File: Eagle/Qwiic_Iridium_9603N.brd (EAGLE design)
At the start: 50.8 x 50.8 mm, 90 parts, among them J1 IRIDIUM_9603N, J3 PTH, J6 ISP, J7 U.FL, Q2 5.8A/30V/35mΩ, U1 ATTINY841SOIC, U2 LTC3225EDDB#TRMPBF, U3 ADM4210-1

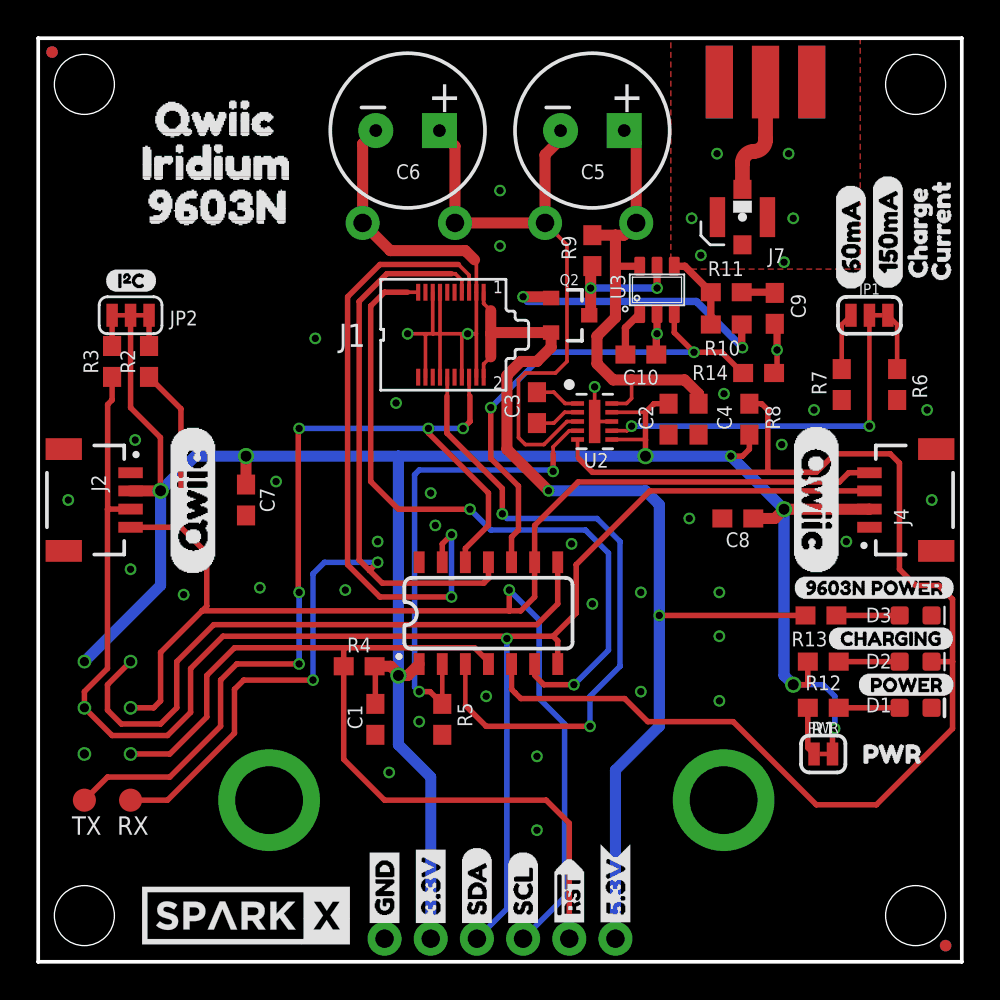
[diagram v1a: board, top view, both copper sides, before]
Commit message: Add ignore. Remove old backup files. Move TPs to bottom of board.
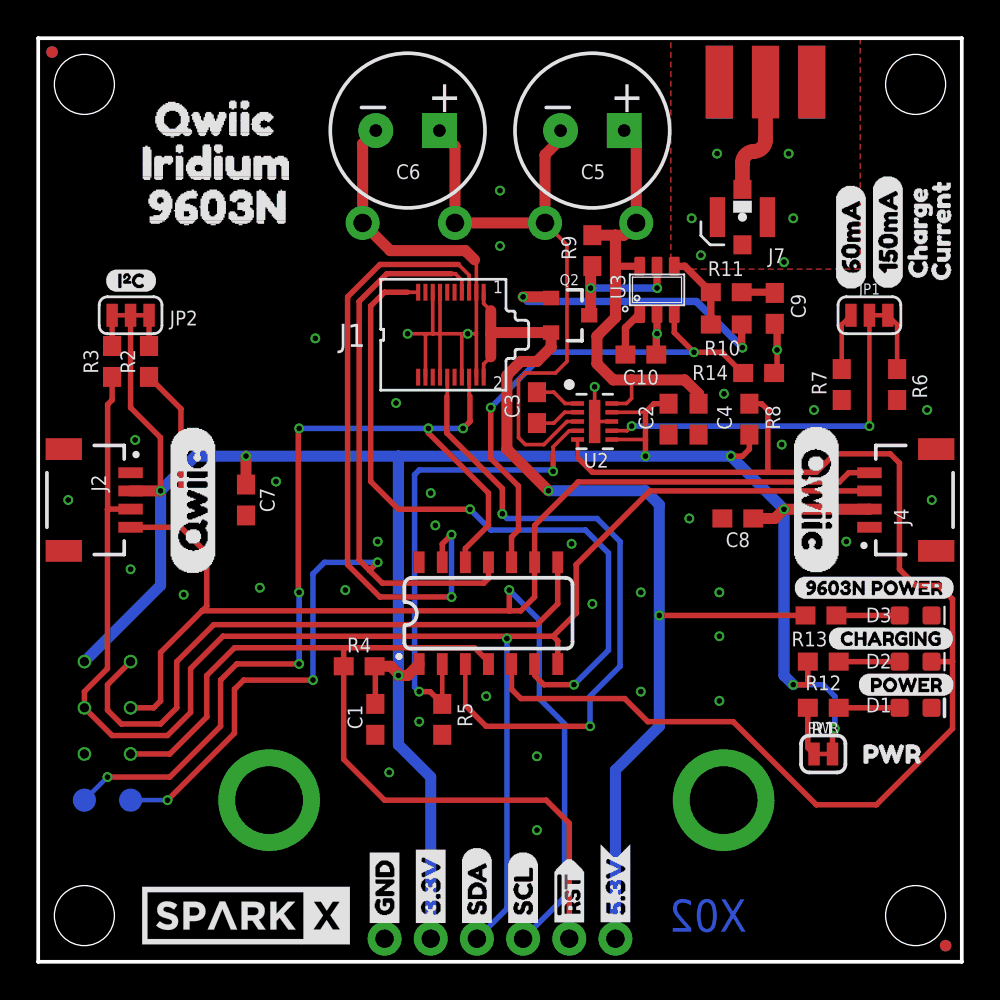
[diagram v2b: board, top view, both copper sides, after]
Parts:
- J2, J4: value (none) -> QWIIC_RIGHT_ANGLE
- flipped RX to the bottom
- flipped TX to the bottom
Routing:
- net RX(OUT): vias 2 -> 3
- net TX(IN): vias 5 -> 6
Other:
- board text added: "X02"
- board text removed: "X0.1"

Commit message: Update connector footprint: reduce cream, extend copper, remove extra silk.
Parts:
- J2, J4: value QWIIC_RIGHT_ANGLE -> (none)
- JP10, JP3, JP4, JP9: device SparkFun:STAND-OFF -> SparkFun-Hardware:STAND-OFF
- JP5, JP6, JP7, JP8: value FIDUCIALUFIDUCIAL -> FIDUCIAL1X2; device SparkFun:MICRO-FIDUCIAL -> SparkFun-Aesthetics:FIDUCIAL-1X2
- R1, R12: device SparkFun-Resistors:0603 -> Qwiic_Iridium_9603N:0603
- U3: device ADM4210:TSOT6 -> Qwiic_Iridium_9603N:TSOT6
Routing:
- net GND: track 42.4 -> 43.0 mm

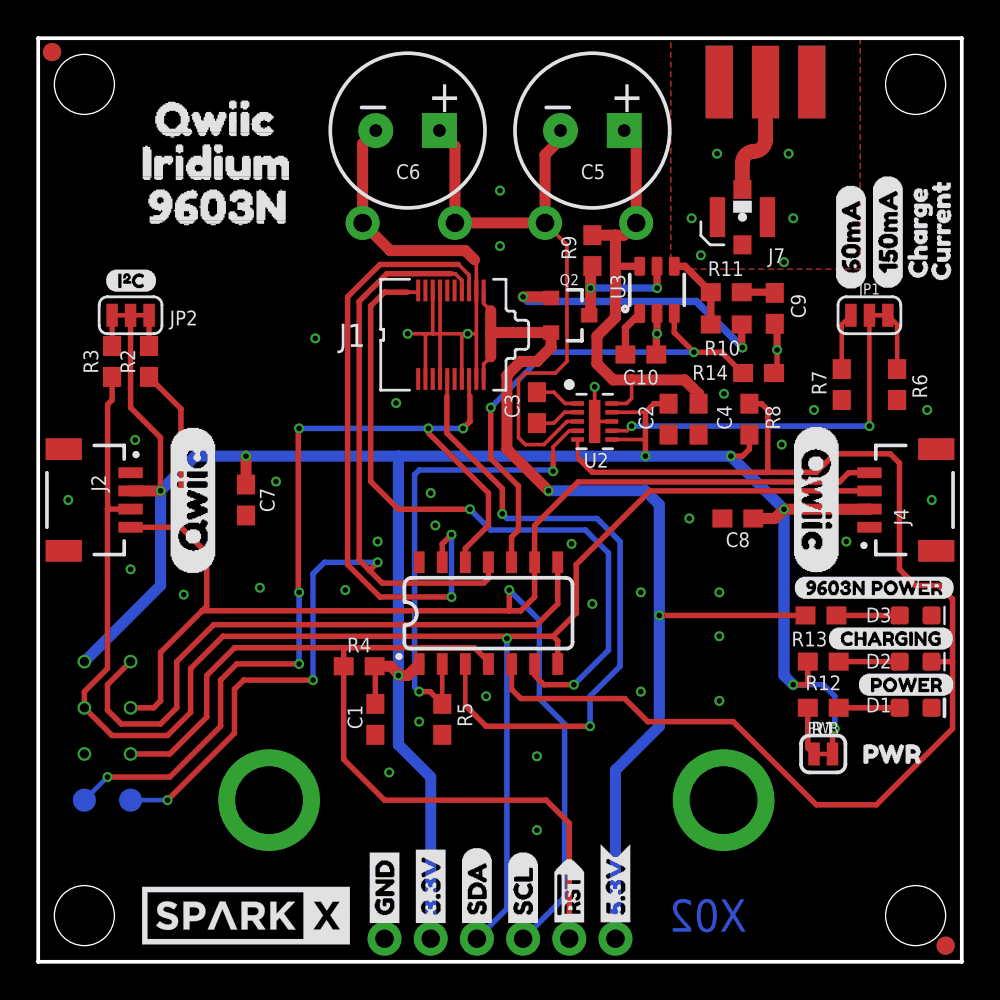
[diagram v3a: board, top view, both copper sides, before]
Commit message: Change connector to use SMD reflowable standoffs
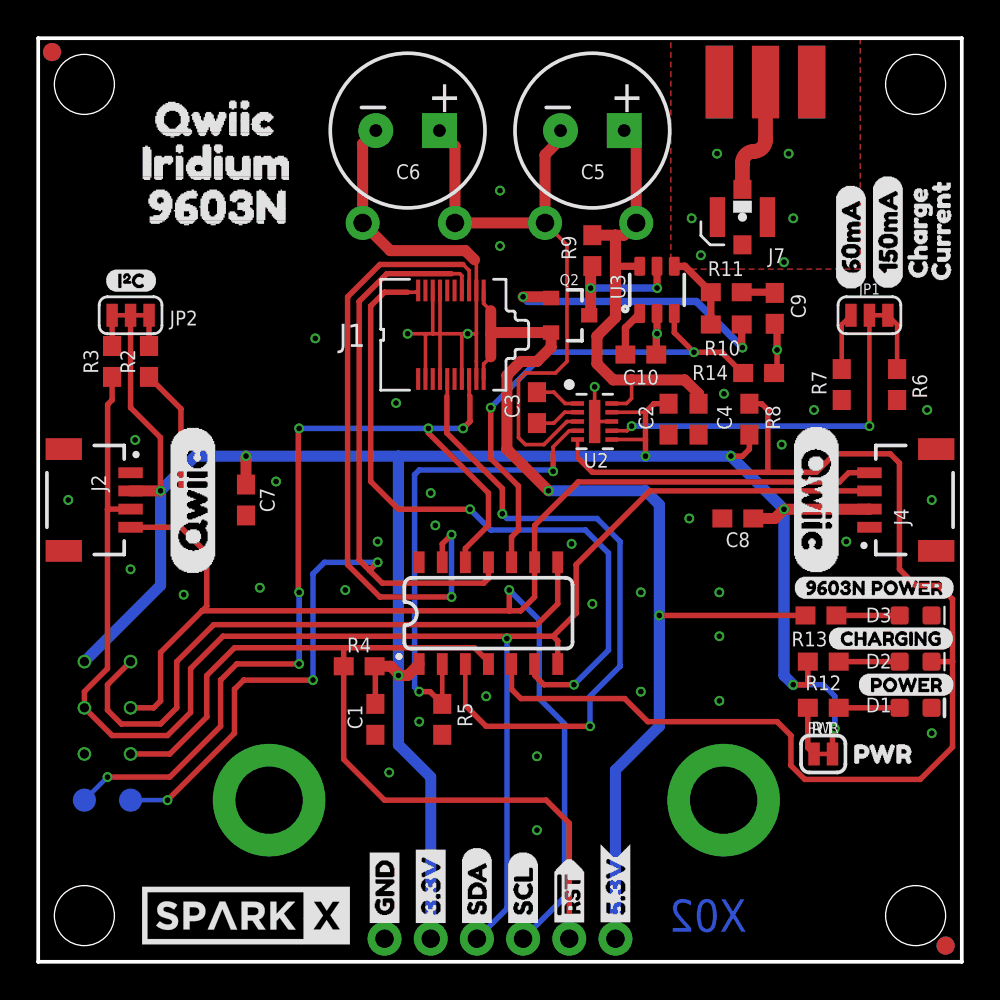
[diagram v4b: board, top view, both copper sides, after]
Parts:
- moved U$31 0.51 mm to (43.6, 11.4)
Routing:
- net GND: vias 44 -> 45
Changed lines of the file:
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@@
 <layer number="44" name="Drills" color="7" fill="1" visible="no" active="yes"/>
 <layer number="45" name="Holes" color="7" fill="1" visible="yes" active="yes"/>
-<layer number="46" name="Milling" color="3" fill="1" visible="yes" active="yes"/>
+<layer number="46" name="Milling" color="3" fill="1" visible="no" active="yes"/>
 <layer number="47" name="Measures" color="7" fill="1" visible="no" active="yes"/>
 <layer number="48" name="Document" color="7" fill="1" visible="no" active="yes"/>
-<layer number="49" name="Reference" color="7" fill="1" visible="no" active="yes"/>
+<layer number="49" name="Reference" color="7" fill="1" visible="yes" active="yes"/>
 <layer number="50" name="dxf" color="7" fill="1" visible="no" active="yes"/>
 <layer number="51" name="tDocu" color="6" fill="1" visible="yes" active="yes"/>
@@
 <element name="U$29" library="SparkX" package="SPARKX-LARGE" value="" x="8.89" y="41.91" smashed="yes" rot="MR0"/>
 <element name="U$30" library="SparkX" package="SPARKX-LARGE" value="" x="11.43" y="2.54" smashed="yes"/>
-<element name="U$31" library="buzzard_labels (7)" package="_PWR1" value="" x="44.069" y="11.43" smashed="yes"/>
+<element name="U$31" library="buzzard_labels (7)" package="_PWR1" value="" x="43.561" y="11.43" smashed="yes"/>
 <element name="U$32" library="buzzard_labels (7)" package="5#3V0" value="" x="31.75" y="1.651" smashed="yes" rot="R90"/>
 <element name="U$11" library="buzzard_labels (7)" package="5#3V0" value="" x="31.75" y="1.651" smashed="yes" rot="MR90"/>
@@
 <contactref element="J1" pad="14"/>
 <contactref element="J1" pad="18"/>
-<wire x1="24.1" y1="32.055" x2="24.1" y2="34.544" width="0.2032" layer="1"/>
+<wire x1="24.1" y1="32.055" x2="24.1" y2="33.02" width="0.2032" layer="1"/>
+<wire x1="24.1" y1="33.02" x2="24.1" y2="34.544" width="0.2032" layer="1"/>
 <wire x1="24.1" y1="34.544" x2="24.1" y2="36.925" width="0.2032" layer="1"/>
 <wire x1="23.622" y1="34.544" x2="24.1" y2="34.544" width="0.2032" layer="1"/>
@@
 <via x="30.607" y="31.623" extent="1-16" drill="0.3048"/>
 <wire x1="30.607" y1="29.718" x2="30.607" y2="31.623" width="0.2032" layer="1"/>
+<wire x1="24.1" y1="33.02" x2="24.1" y2="33.02" width="0.2032" layer="1"/>
+<via x="49.149" y="12.573" extent="1-16" drill="0.3048"/>
 </signal>
 <signal name="SCL">
@@
 <wire x1="17.018" y1="36.576" x2="17.018" y2="21.844" width="0.3048" layer="1"/>
 <wire x1="17.018" y1="36.576" x2="18.796" y2="38.354" width="0.3048" layer="1"/>
-<wire x1="18.796" y1="38.354" x2="23.114" y2="38.354" width="0.3048" layer="1"/>
-<wire x1="23.69998125" y1="37.76801875" x2="23.114" y2="38.354" width="0.2032" layer="1"/>
+<wire x1="18.796" y1="38.354" x2="23.368" y2="38.354" width="0.3048" layer="1"/>
+<wire x1="23.69998125" y1="38.02201875" x2="23.368" y2="38.354" width="0.2032" layer="1"/>
 <contactref element="J1" pad="5"/>
 <wire x1="23.7" y1="36.925" x2="23.69998125" y2="36.82501875" width="0.2032" layer="1"/>
-<wire x1="23.69998125" y1="36.82501875" x2="23.69998125" y2="37.76801875" width="0.2032" layer="1"/>
+<wire x1="23.69998125" y1="36.82501875" x2="23.69998125" y2="38.02201875" width="0.2032" layer="1"/>
 <wire x1="18.796" y1="20.066" x2="22.733" y2="20.066" width="0.3048" layer="1"/>
 <via x="22.733" y="20.066" extent="1-16" drill="0.3048"/>
@@
 </signal>
 <signal name="RX(OUT)">
-<wire x1="22.733" y1="37.846" x2="22.93823125" y2="37.846" width="0.2032" layer="1"/>
-<wire x1="23.29998125" y1="37.48425" x2="22.93823125" y2="37.846" width="0.2032" layer="1"/>
+<wire x1="22.733" y1="37.846" x2="23.19223125" y2="37.846" width="0.2032" layer="1"/>
+<wire x1="23.29998125" y1="37.73825" x2="23.19223125" y2="37.846" width="0.2032" layer="1"/>
 <wire x1="18.923" y1="20.828" x2="18.2245" y2="21.5265" width="0.3048" layer="1"/>
 <wire x1="18.2245" y1="21.5265" x2="17.653" y2="22.098" width="0.3048" layer="1"/>
@@
 <contactref element="J1" pad="7"/>
 <wire x1="23.3" y1="36.925" x2="23.29998125" y2="36.82501875" width="0.2032" layer="1"/>
-<wire x1="23.29998125" y1="36.82501875" x2="23.29998125" y2="37.48425" width="0.2032" layer="1"/>
+<wire x1="23.29998125" y1="36.82501875" x2="23.29998125" y2="37.73825" width="0.2032" layer="1"/>
 <wire x1="24.511" y1="20.828" x2="24.765" y2="21.082" width="0.3048" layer="1"/>
 <wire x1="24.511" y1="20.828" x2="18.923" y2="20.828" width="0.3048" layer="1"/>
@@
 <wire x1="48.26" y1="20.701" x2="49.53" y2="20.701" width="0.3048" layer="1"/>
 <wire x1="49.53" y1="20.701" x2="50.292" y2="19.939" width="0.3048" layer="1"/>
-<wire x1="50.292" y1="12.827" x2="46.101" y2="8.636" width="0.3048" layer="1"/>
-<wire x1="46.101" y1="8.636" x2="42.799" y2="8.636" width="0.3048" layer="1"/>
-<wire x1="42.799" y1="8.636" x2="38.227" y2="13.208" width="0.3048" layer="1"/>
-<wire x1="33.528" y1="13.208" x2="38.227" y2="13.208" width="0.3048" layer="1"/>
+<wire x1="50.292" y1="11.811" x2="48.514" y2="10.033" width="0.3048" layer="1"/>
+<wire x1="42.164" y1="10.033" x2="48.514" y2="10.033" width="0.3048" layer="1"/>
 <wire x1="30.48" y1="26.924" x2="40.132" y2="26.924" width="0.3048" layer="1"/>
 <wire x1="40.132" y1="26.924" x2="42.799" y2="26.924" width="0.3048" layer="1"/>
 <wire x1="50.292" y1="19.939" x2="50.292" y2="16.51" width="0.3048" layer="1"/>
-<wire x1="50.292" y1="16.51" x2="50.292" y2="12.827" width="0.3048" layer="1"/>
+<wire x1="50.292" y1="16.51" x2="50.292" y2="11.811" width="0.3048" layer="1"/>
 <wire x1="49.137" y1="16.51" x2="50.292" y2="16.51" width="0.3048" layer="1"/>
 <wire x1="39.116" y1="30.695" x2="39.79" y2="30.695" width="0.3048" layer="1"/>
@@
 <contactref element="U1" pad="5"/>
 <wire x1="26.035" y1="14.986" x2="26.035" y2="16.377" width="0.3048" layer="1"/>
+<wire x1="41.402" y1="12.446" x2="41.402" y2="10.795" width="0.3048" layer="1"/>
+<wire x1="41.402" y1="10.795" x2="42.164" y2="10.033" width="0.3048" layer="1"/>
+<wire x1="33.528" y1="13.208" x2="40.64" y2="13.208" width="0.3048" layer="1"/>
+<wire x1="40.64" y1="13.208" x2="41.402" y2="12.446" width="0.3048" layer="1"/>
 </signal>
 <signal name="N$11">
@@
 <via x="29.464" y="15.24" extent="1-16" drill="0.3048"/>
 <contactref element="J1" pad="19"/>
-<wire x1="20.9" y1="36.925" x2="20.895" y2="36.83" width="0.2032" layer="1"/>
-<wire x1="20.895" y1="36.83" x2="20.32" y2="36.83" width="0.2032" layer="1"/>
 <contactref element="U1" pad="6"/>
 <wire x1="27.813" y1="15.24" x2="27.305" y2="15.748" width="0.3048" layer="1"/>
 <wire x1="27.305" y1="15.748" x2="27.305" y2="16.377" width="0.254" layer="1"/>
+<wire x1="20.9" y1="36.925" x2="20.805" y2="36.83" width="0.2032" layer="1"/>
+<wire x1="20.805" y1="36.83" x2="20.32" y2="36.83" width="0.2032" layer="1"/>
 </signal>
 <signal name="N$7">
